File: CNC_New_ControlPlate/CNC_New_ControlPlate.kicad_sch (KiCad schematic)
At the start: 11 parts, among them J1 OTHER, U1 PC847

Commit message: +Файл линий HOME и SENSOR
+ Завел датчики через оптопары
+ Посчитал токоограничивающие резисторы на вход и выход оптопары
+ Поставил стабилитроны, возможно не понадобятся
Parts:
- removed D1, D? (x3): D_Zener, symbol Device:D_Zener
- removed FB1, FB? (x3): FerriteBead, symbol Device:FerriteBead
- removed U1: PC847, Package_DIP:DIP-16_W7.62mm, symbol Isolator:PC847
- J1: value OTHER -> (none)
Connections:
- net GND: no longer J1.6 (Pin_6)
- net GNDREF: now also J1.6 (Pin_6)
- net 3.3V renamed +3V3
- net VCC renamed +5V
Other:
- added sheet HOME optocouplers (home_optocouplers.kicad_sch)

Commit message: Датчики и щуп через оптопары
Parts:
- J1: value (none) -> OTHER
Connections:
- net Probe_5V renamed SENSOR_3.3V
- net X_Limit_5V renamed Z_HOME_3.3V
- net Y_Limit_5V renamed Y_HOME_3.3V
- net Z_Limit_5V renamed X_HOME_3.3V

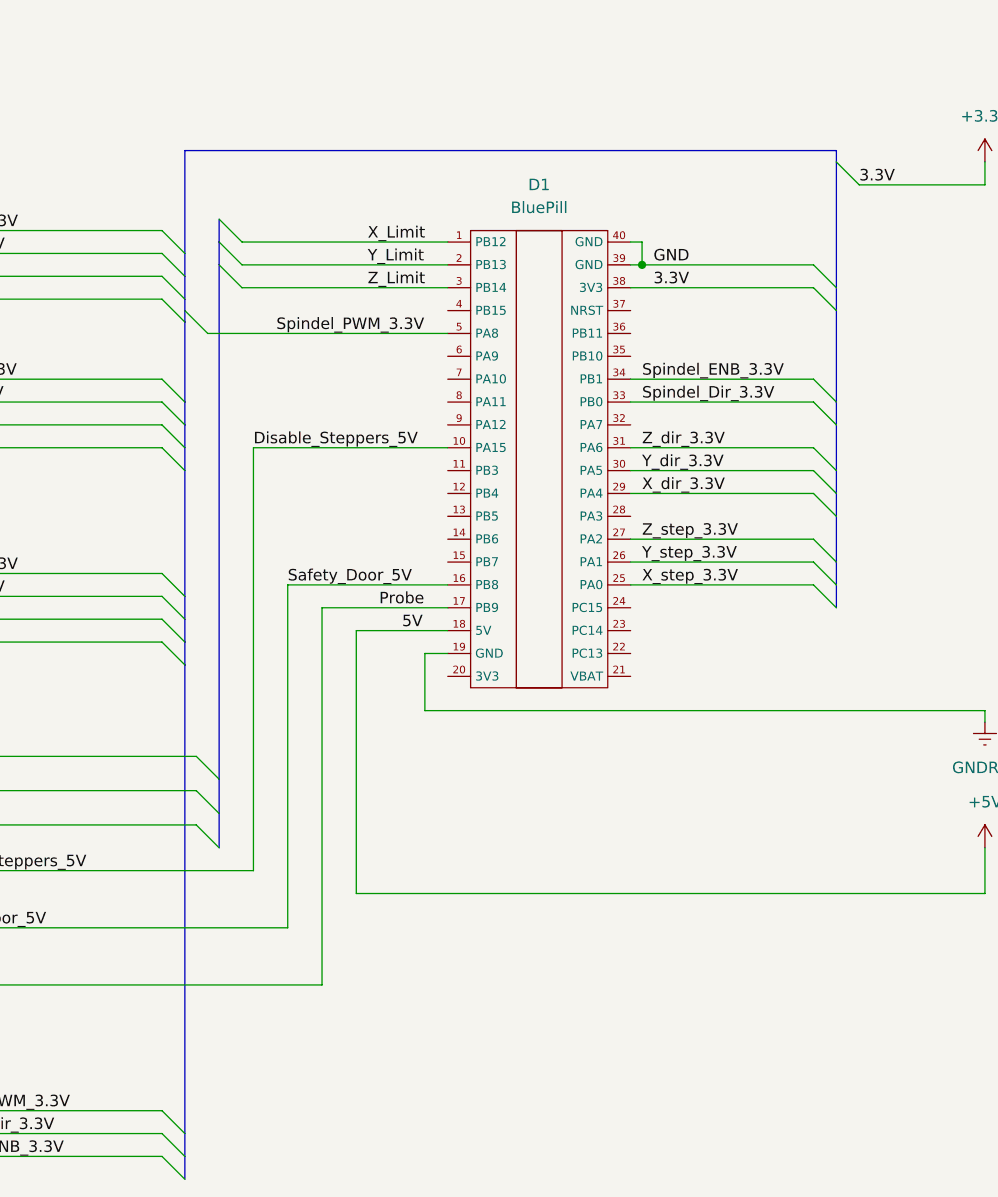
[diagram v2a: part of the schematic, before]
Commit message: Обновил датчики HOME
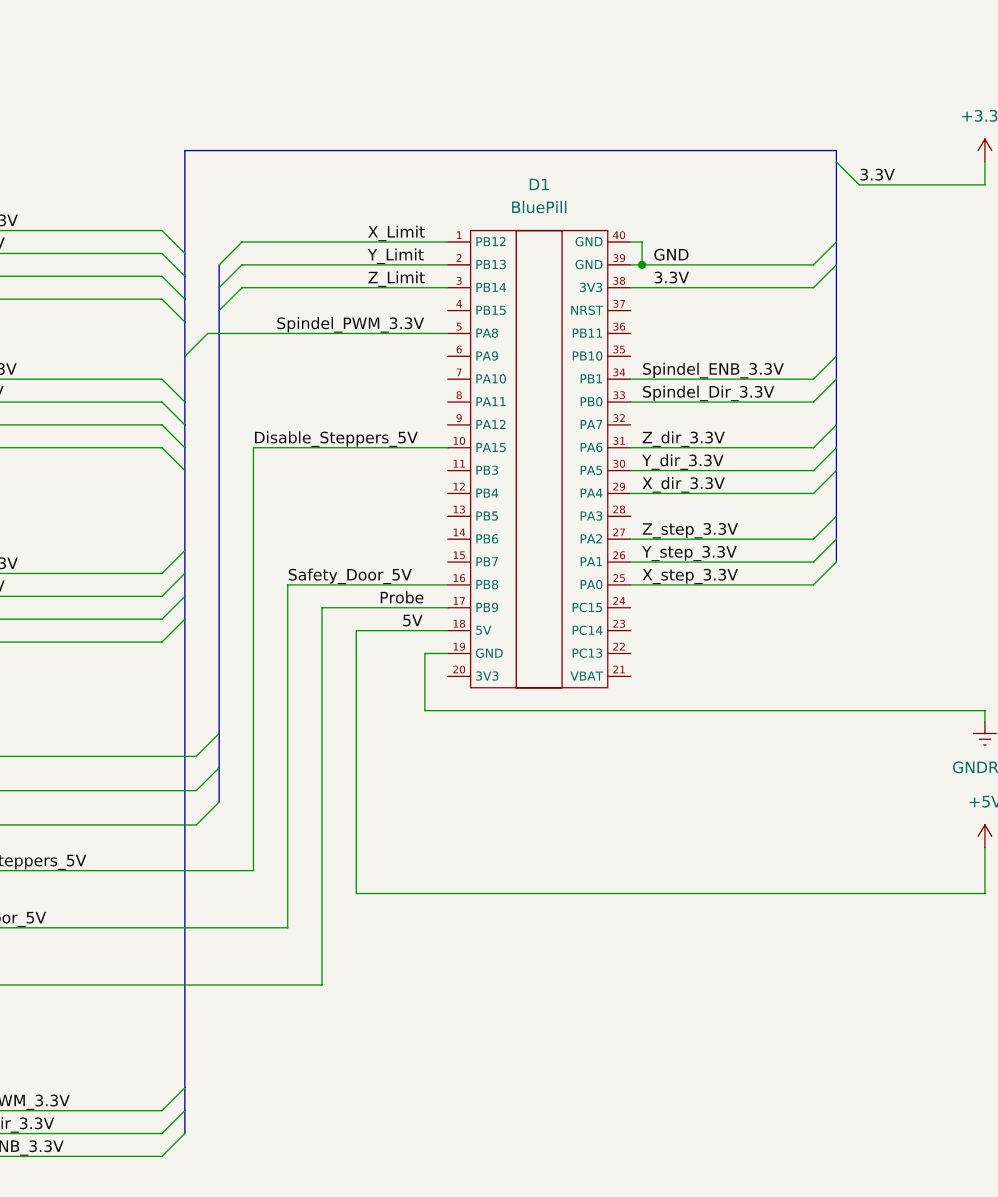
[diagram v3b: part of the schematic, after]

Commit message: [+] Лист STEPPERS [+] Разъем подключения шаговиков [+] Моделька драйвера дифф линий [+] Управление X Y заведено через драйверы дифф линий [+] Управление Z заведено через инвертор [+] Enable Z заведен через инвертор к Disable Steppers
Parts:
- removed D1: BluePill, Module:Maple_Mini, symbol G-LIB:BP
- added D?: (no value), symbol EP2006:Blue_Pill
- added J?: (no value), symbol Connector_Generic:Conn_02x09_Odd_Even
- J1: value OTHER -> (none)
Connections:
- net +3V3: now also D?.38 (3V3)
- net +5V: now also D?.18 (5V), J?.11 (Pin_11), J?.17 (Pin_17), J?.5 (Pin_5)
- net GNDREF: now also D?.19 (GND), D?.39 (GND), D?.40 (GND)
- net SENSOR_3.3V: now also D?.17 (PB9)
- net Safety_Door_5V: now also D?.16 (PB8)
- net Spindel_Dir_3.3V: now also D?.33 (PB0)
- net Spindel_ENB_3.3V: now also D?.34 (PB1)
- net Spindel_PWM_3.3V: now also D?.5 (PA8)
- net X_HOME_3.3V: now also D?.3 (PB14)
- net Y_HOME_3.3V: now also D?.2 (PB13)
- net Z_HOME_3.3V: now also D?.1 (PB12)
- new net X_DIR_3.3V: D?.29 (PA4)
- new net X_DIR_n: J?.4 (Pin_4)
- new net X_DIR_p: J?.3 (Pin_3)
- new net X_STEP_3.3V: D?.25 (PA0)
- new net X_STEP_n: J?.2 (Pin_2)
- new net X_STEP_p: J?.1 (Pin_1)
- new net Y_DIR_3.3V: D?.30 (PA5)
- new net Y_DIR_n: J?.10 (Pin_10)
- new net Y_DIR_p: J?.9 (Pin_9)
- new net Y_STEP_3.3V: D?.26 (PA1)
- new net Y_STEP_n: J?.8 (Pin_8)
- new net Y_STEP_p: J?.7 (Pin_7)
- new net Z1n: J?.14 (Pin_14)
- new net Z2n: J?.16 (Pin_16)
- new net Z_DIR: J?.15 (Pin_15)
- new net Z_DIR_3.3V: D?.31 (PA6)
- new net Z_EN: J?.6 (Pin_6)
- new net Z_EN_3.3V: D?.10 (PA15)
- new net Z_STEP: J?.13 (Pin_13)
- new net Z_STEP_3.3V: D?.27 (PA2)
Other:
- added sheet Steppers (steppers.kicad_sch)
- moved on the sheet: J1

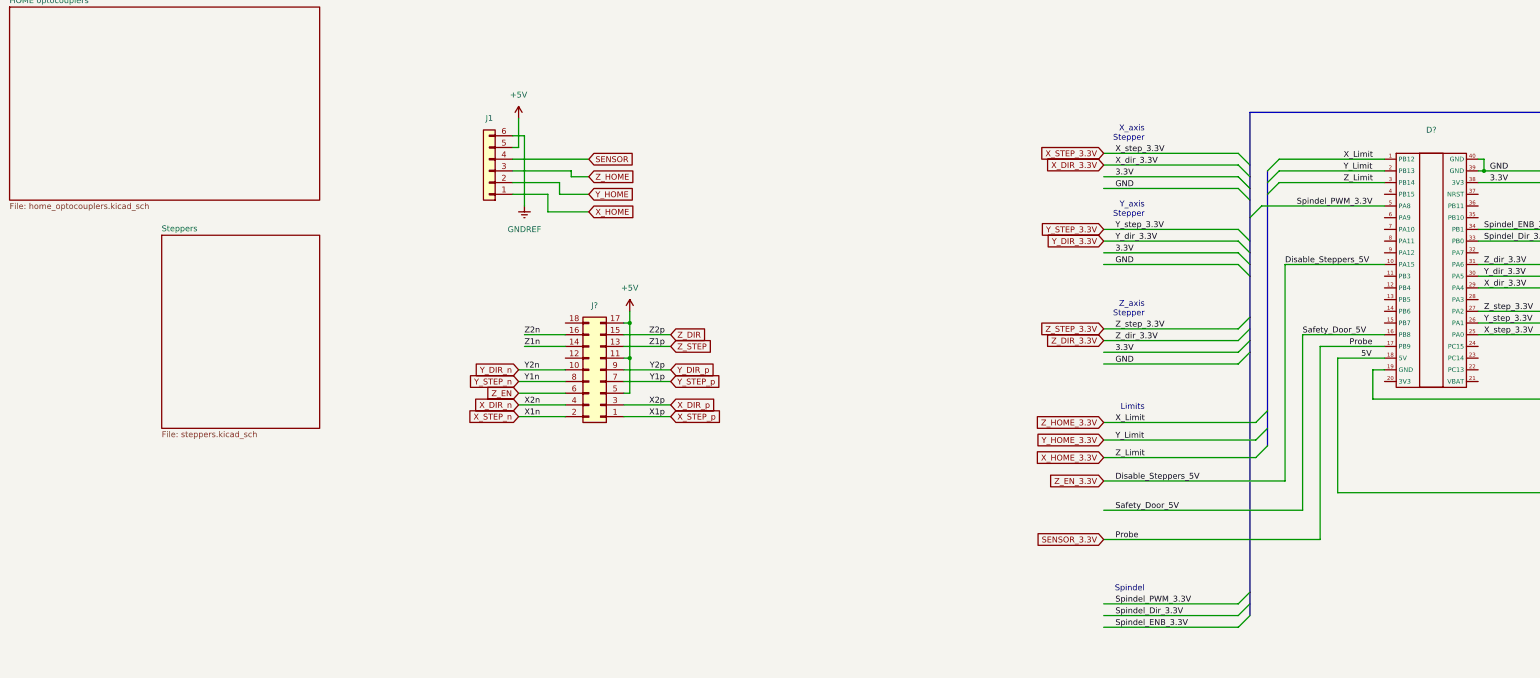
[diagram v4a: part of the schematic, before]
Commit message: Add spindel sch
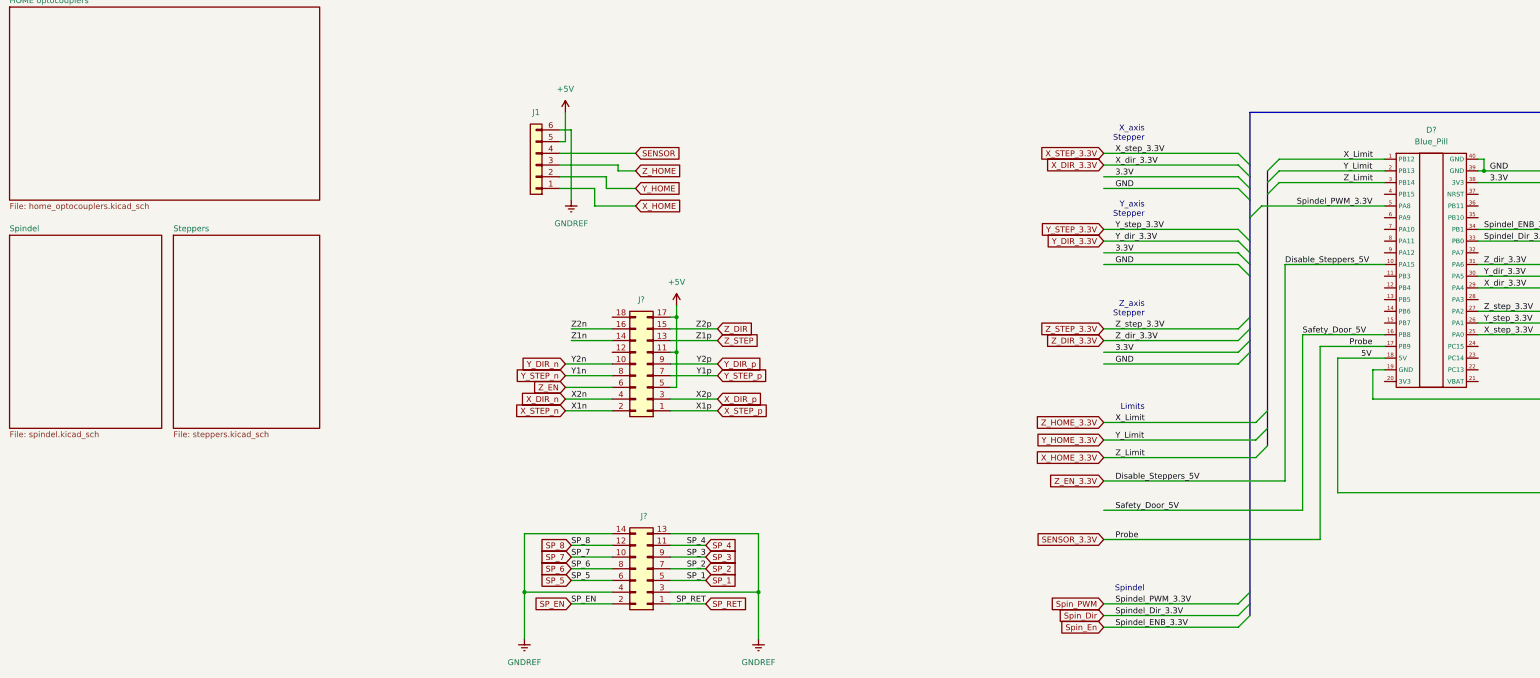
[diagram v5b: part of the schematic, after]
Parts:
- added J?: (no value), symbol Connector_Generic:Conn_02x07_Odd_Even
- D?: value (none) -> Blue_Pill; footprint (none) -> Module:Maple_Mini
- J1: value (none) -> OTHER
- J?: value (none) -> STEPPERS
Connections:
- net GNDREF: now also J?.13 (Pin_13), J?.14 (Pin_14), J?.3 (Pin_3), J?.4 (Pin_4)
- net Spindel_Dir_3.3V renamed Spin_Dir
- net Spindel_ENB_3.3V renamed Spin_En
- net Spindel_PWM_3.3V renamed Spin_PWM
- new net SP_1: J?.5 (Pin_5)
- new net SP_2: J?.7 (Pin_7)
- new net SP_3: J?.9 (Pin_9)
- new net SP_4: J?.11 (Pin_11)
- new net SP_5: J?.6 (Pin_6)
- new net SP_6: J?.8 (Pin_8)
- new net SP_7: J?.10 (Pin_10)
- new net SP_8: J?.12 (Pin_12)
- new net SP_EN: J?.2 (Pin_2)
- new net SP_RET: J?.1 (Pin_1)
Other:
- added sheet Spindel (spindel.kicad_sch)
- moved on the sheet: J1, J?

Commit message: Add attiny2313
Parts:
- J?: value (none) -> SPINDEL
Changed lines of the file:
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@@
       (effects (font (size 1.27 1.27)) (justify left))
     )
-    (property "Value" "" (id 1) (at 55.8799 132.08 90)
+    (property "Value" "SPINDEL" (id 1) (at 55.8799 132.08 90)
       (effects (font (size 1.27 1.27)) (justify left) hide)
     )
@@
       (reference "U?") (unit 1) (value "7406") (footprint "")
     )
+    (path "/f81b86d1-c1b9-4e8d-8ec5-902244442743/9f735f94-c12e-4d19-924f-16af0f881e41"
+      (reference "U?") (unit 1) (value "ATtiny2313V-10P") (footprint "Package_DIP:DIP-20_W7.62mm")
+    )
     (path "/cddb5583-7ddf-474c-aeca-fbc0e04243fc/3d75ff4a-fbad-4181-b5f4-65bd16a4fd34"
